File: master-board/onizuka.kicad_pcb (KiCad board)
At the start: 2 copper layers, 50 x 50 mm, 27 parts, among them IC1 FT232RQ, IC2 ADCMP371, P1 USB_OTG, P2 FTDI, P3 EXTRA, Q1 Q_PMOS_DGS, SW1 SWITCH_INV, U1 LD1117S33TR

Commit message: ESP8266 daughter board
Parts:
- moved R4 55.9 mm to (56.8, 25.4), turned to 270 degrees
- moved C3 50.5 mm to (45.8, 29.0), turned to 90 degrees
- moved SW1 49.5 mm to (55.2, 36.8)
- moved D2 48.9 mm to (43.6, 31.2), turned to 180 degrees
- moved R2 48.9 mm to (46.4, 31.2)
- moved D1 47.3 mm to (43.6, 32.8), turned to 180 degrees
- moved R1 47.3 mm to (46.4, 32.8)
- moved R6 46.2 mm to (51.4, 34.3)
- moved R5 45.9 mm to (48.8, 34.3)
- moved C2 45.7 mm to (47.4, 29.0), turned to 90 degrees
- moved IC2 43.8 mm to (50.2, 36.6), turned to 180 degrees
- moved C1 41.2 mm to (49.8, 26.7), turned to 180 degrees
- moved R3 38.8 mm to (34.5, 42.7), turned to 180 degrees
- moved D3 37.5 mm to (38.9, 43.1)
- moved U1 34.4 mm to (57.9, 41.9), turned to 270 degrees
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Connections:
- IC1 pad 33: (no net) -> GND
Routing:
- net +5V: track 0.00 -> 38.1 mm, vias 0 -> 4
- net /RI: track 0.00 -> 21.2 mm, vias 0 -> 2
- net /DCD: track 0.15 -> 21.3 mm, vias 0 -> 2
- net /VCCIO: track 0.00 -> 20.6 mm, vias 0 -> 2
- net /DSR: track 0.00 -> 19.4 mm, vias 0 -> 2
- net /TXD: track 0.15 -> 19.1 mm, vias 0 -> 1
- net GND: track 0.00 -> 17.8 mm, vias 0 -> 10
- net /DTR: track 0.00 -> 13.7 mm
- net /CTS: track 0.00 -> 12.4 mm
- net /RTS: track 1.32 -> 13.4 mm
- net /RXD: track 0.15 -> 10.7 mm
- net /PWROUT: track 3.07 -> 10.3 mm, vias 0 -> 1
- net +3V3: track 0.00 -> 6.40 mm
- net /PWREN: track 0.00 -> 4.51 mm
- net /TXLED: track 0.00 -> 4.34 mm
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- added copper zone on B.Cu, net GND

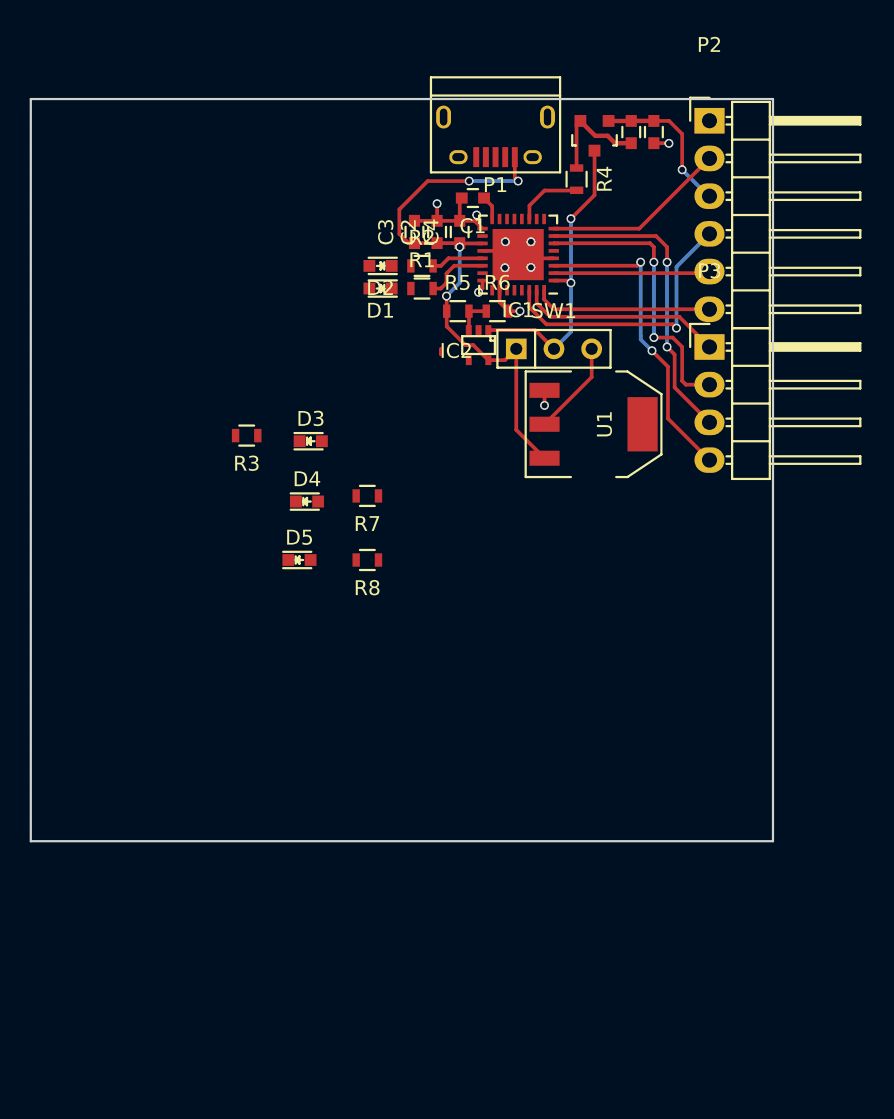
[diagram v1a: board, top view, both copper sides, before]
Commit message: Slight schematic rework, much PCB faffing
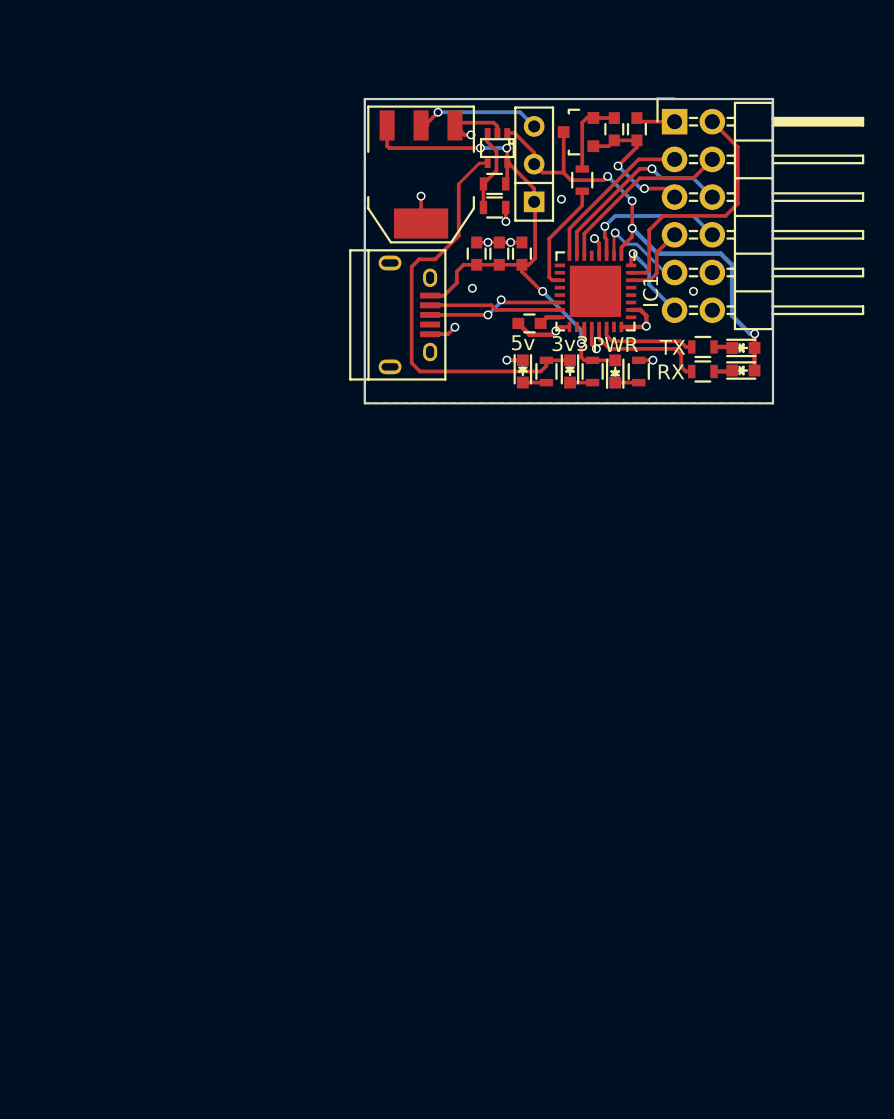
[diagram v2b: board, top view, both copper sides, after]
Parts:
- removed P3: EXTRA, Pin_Headers:Pin_Header_Angled_1x04
- P2: footprint Pin_Headers:Pin_Header_Angled_1x06 -> Pin_Headers:Pin_Header_Angled_2x06
- moved R3 26.8 mm to (61.0, 38.4), turned to 90 degrees
- moved D2 25.4 mm to (68.0, 38.3), turned to 0 degrees
- moved D1 24.8 mm to (68.0, 36.8), turned to 0 degrees
- moved D3 21.0 mm to (59.4, 38.4), turned to 90 degrees
- moved U1 20.4 mm to (46.3, 25.1), turned to 180 degrees
- moved R2 20.2 mm to (65.3, 38.4), turned to 180 degrees
- moved D4 19.8 mm to (56.3, 38.4), turned to 270 degrees
- moved D5 19.7 mm to (53.1, 38.4), turned to 270 degrees
- moved R1 19.3 mm to (65.3, 36.7), turned to 180 degrees
- moved R8 17.5 mm to (54.7, 38.4), turned to 270 degrees
- moved R7 17.3 mm to (57.8, 38.4), turned to 270 degrees
- moved P1 13.6 mm to (45.3, 34.5), turned to 270 degrees
- moved IC2 13.3 mm to (51.4, 23.3)
- moved SW1 12.5 mm to (53.9, 24.4), turned to 90 degrees
- moved C1 9.27 mm to (53.6, 35.1)
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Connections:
- IC1 pad 10: (no net) -> Net-(IC1-Pad10)
- IC1 pad 12: (no net) -> Net-(IC1-Pad12)
- IC1 pad 13: (no net) -> Net-(IC1-Pad13)
- IC1 pad 18: (no net) -> Net-(IC1-Pad18)
- IC1 pad 23: (no net) -> Net-(IC1-Pad23)
- IC1 pad 25: (no net) -> Net-(IC1-Pad25)
- IC1 pad 27: (no net) -> Net-(IC1-Pad27)
- IC1 pad 28: (no net) -> Net-(IC1-Pad28)
- IC1 pad 29: (no net) -> Net-(IC1-Pad29)
- IC1 pad 33: GND -> (no net)
- IC1 pad 5: (no net) -> Net-(IC1-Pad5)
- IC1 pad 9: (no net) -> Net-(IC1-Pad9)
- P1 pad 4: (no net) -> Net-(P1-Pad4)
- P1 pad 6: Net-(P1-Pad6) -> GND
- P2 pad 2: /CTS -> /DTR
- P2 pad 3: /PWROUT -> /CTS
- P2 pad 4: /TXD -> /DSR
- P2 pad 5: /RXD -> /PWROUT
- P2 pad 6: /RTS -> /DCD
- U1 pad 4: (no net) -> GND
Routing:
- net Net-(D4-Pad1): track 0.00 -> 28.0 mm
- net /TXD: track 19.1 -> 5.02 mm, vias 1 -> 0
- net /VCCIO: track 20.6 -> 33.5 mm, vias 2 -> 4
- net /RI: track 21.2 -> 10.1 mm, vias 2 -> 1
- net GND: track 17.8 -> 28.3 mm, vias 10 -> 15
- net Net-(IC1-Pad14): track 0.00 -> 9.78 mm, vias 0 -> 2
- net Net-(IC1-Pad15): track 0.00 -> 9.34 mm
- net /DCD: track 21.3 -> 13.3 mm, vias 2 -> 1
- net /RTS: track 13.4 -> 5.82 mm, vias 0 -> 1
- net /DSR: track 19.4 -> 12.2 mm, vias 2 -> 0
- net /RXLED: track 3.54 -> 8.42 mm
- net /RXD: track 10.7 -> 6.74 mm, vias 0 -> 1
- net Net-(IC2-Pad3): track 2.44 -> 5.66 mm
- net /DTR: track 13.7 -> 16.9 mm
- net /PWREN: track 4.51 -> 7.51 mm
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- added copper zone on F.Cu, net GND
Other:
- board size 50 x 50 mm -> 27.5 x 20.5 mm

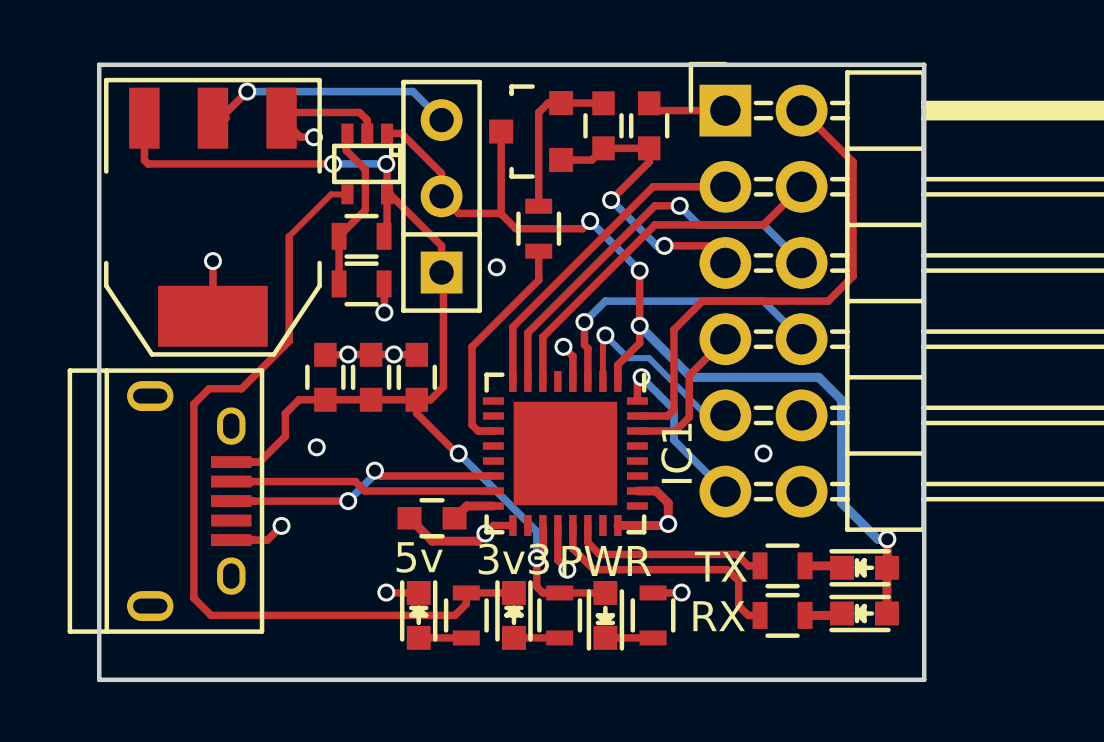
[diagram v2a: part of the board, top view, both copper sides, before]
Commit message: Various upgrades, also ESP-12E footprint for ESP board
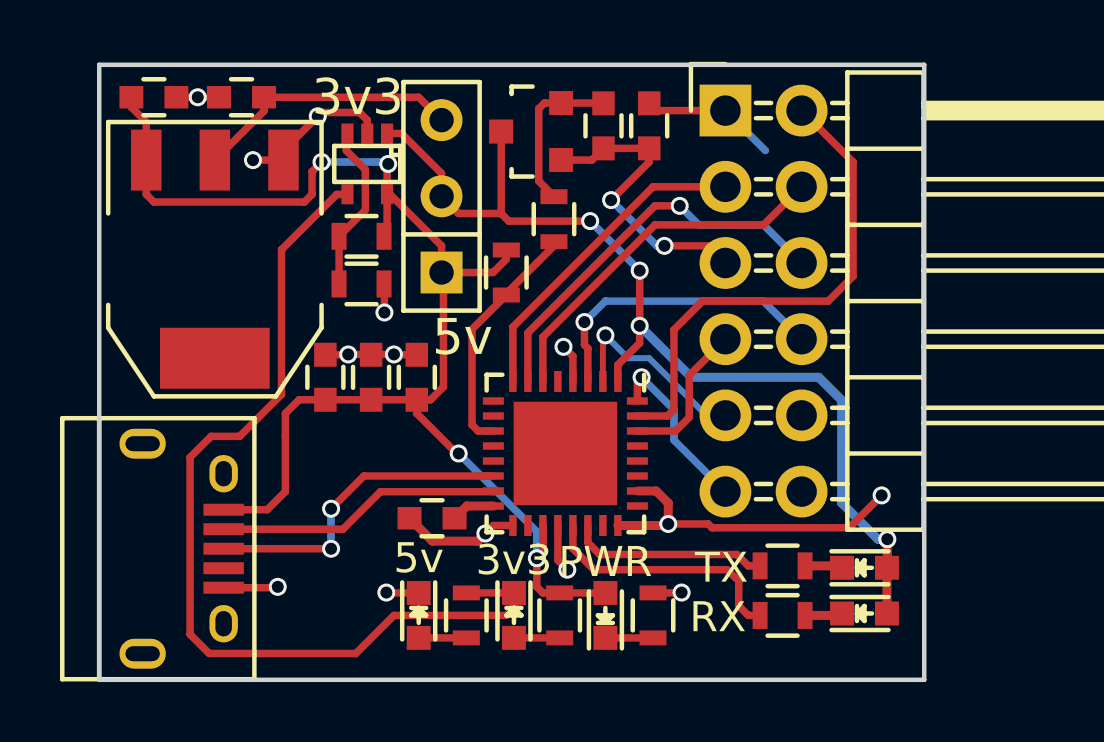
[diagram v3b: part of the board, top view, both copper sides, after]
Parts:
- added C7: 100n, Capacitors_SMD:C_0603, F.Cu at (44.3, 21.1)
- added C8: 10u, Capacitors_SMD:C_0603, F.Cu at (47.2, 21.1)
- added R9: 10k, Resistors_SMD:R_0603, F.Cu at (56.1, 26.9)
- moved P1 1.61 mm to (45.1, 36.1)
- moved U1 1.40 mm to (46.4, 26.5)
- moved R4 0.60 mm to (57.7, 25.1)
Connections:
- net Net-(D4-Pad1) renamed /LEDCTRL
- net Net-(IC1-Pad14) renamed /USBD+
- net Net-(IC1-Pad15) renamed /USBD-
- net Net-(IC2-Pad3) renamed /4v5
- U1 pad 4: GND -> (no net)
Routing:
- net GND: track 28.3 -> 37.2 mm, vias 15 -> 14
- net +5V: track 40.6 -> 47.9 mm
- net /LEDCTRL: track 28.0 -> 31.4 mm
- net /USBD+: track 9.78 -> 10.8 mm
- net /PWREN: track 7.51 -> 8.03 mm
- net +3V3: track 8.64 -> 9.01 mm, vias 1 -> 0
- removed copper zone on F.Cu, net GND
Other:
- board text added: "3v3"
- board text added: "5v"

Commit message: More faffing
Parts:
- moved C2 5.17 mm to (49.0, 35.5), turned to 270 degrees
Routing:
- net /USBD+: track 10.8 -> 10.00 mm
- net GND: vias 14 -> 13
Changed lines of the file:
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@@
     (links 70)
     (no_connects 0)
-    (area 42.424999 19.924999 70.075001 40.575001)
+    (area 39.16 15.3015 76.798001 41.229)
     (thickness 1.6)
     (drawings 6)
-    (tracks 272)
+    (tracks 269)
     (zones 0)
     (modules 29)
@@
   )
   (module Capacitors_SMD:C_0603 (layer F.Cu)
-    (at 50.038 30.4165 90)
+    (at 49.022 35.4838 270)
     (descr "Capacitor SMD 0603, reflow soldering, AVX (see smccp.pdf)")
     (tags "capacitor 0603")
     (attr smd)
-    (fp_text reference C2 (at 0 -1.9 90) (layer F.SilkS) hide
-      (effects (font (size 1 1) (thickness 0.15)))
-    )
-    (fp_text value 10n (at 0 1.9 90) (layer F.Fab) hide
+    (fp_text reference C2 (at 0 -1.9 270) (layer F.SilkS) hide
+      (effects (font (size 1 1) (thickness 0.15)))
+    )
+    (fp_text value 10n (at 0 1.9 270) (layer F.Fab) hide
       (effects (font (size 1 1) (thickness 0.15)))
     )
@@
     (fp_line (start -0.35 -0.6) (end 0.35 -0.6) (layer F.SilkS) (width 0.15))
     (fp_line (start 0.35 0.6) (end -0.35 0.6) (layer F.SilkS) (width 0.15))
-    (pad 1 smd rect (at -0.75 0 90) (size 0.8 0.75) (layers F.Cu F.Paste F.Mask)
+    (pad 1 smd rect (at -0.75 0 270) (size 0.8 0.75) (layers F.Cu F.Paste F.Mask)
       (net 3 +5V))
-    (pad 2 smd rect (at 0.75 0 90) (size 0.8 0.75) (layers F.Cu F.Paste F.Mask)
+    (pad 2 smd rect (at 0.75 0 270) (size 0.8 0.75) (layers F.Cu F.Paste F.Mask)
       (net 2 GND))
     (model Capacitors_SMD.3dshapes/C_0603.wrl
@@
   (segment (start 54.344 35.1155) (end 54.753 34.7065) (width 0.3) (layer F.Cu) (net 1))
   (segment (start 54.753 34.7065) (end 55.639 34.7065) (width 0.3) (layer F.Cu) (net 1))
+  (segment (start 46.65124 37.4269) (end 48.5521 37.4269) (width 0.25) (layer F.Cu) (net 2))
+  (segment (start 49.022 36.957) (end 48.5521 37.4269) (width 0.25) (layer F.Cu) (net 2))
+  (via (at 48.5521 37.4269) (size 0.6) (drill 0.4) (layers F.Cu B.Cu) (net 2))
+  (segment (start 49.022 36.957) (end 49.022 36.2338) (width 0.25) (layer F.Cu) (net 2))
+  (segment (start 46.65124 37.4269) (end 46.64754 37.4306) (width 0.25) (layer F.Cu) (net 2))
   (segment (start 61.468 35.306) (end 62.8015 35.306) (width 0.25) (layer F.Cu) (net 2))
   (via (at 68.58 34.3535) (size 0.6) (drill 0.4) (layers F.Cu B.Cu) (net 2))
@@
   (via (at 45.7835 21.082) (size 0.6) (drill 0.4) (layers F.Cu B.Cu) (net 2))
   (segment (start 45.7835 21.082) (end 45.073 21.082) (width 0.25) (layer F.Cu) (net 2))
-  (segment (start 46.64754 37.4306) (end 48.4214 37.4306) (width 0.25) (layer F.Cu) (net 2))
-  (via (at 48.4505 37.4015) (size 0.6) (drill 0.4) (layers F.Cu B.Cu) (net 2))
-  (segment (start 48.4214 37.4306) (end 48.4505 37.4015) (width 0.25) (layer F.Cu) (net 2))
   (segment (start 57.789 35.3565) (end 57.789 36.5165) (width 0.25) (layer F.Cu) (net 2))
   (via (at 58.1025 36.83) (size 0.6) (drill 0.4) (layers F.Cu B.Cu) (net 2))
@@
   (via (at 52.324 29.6545) (size 0.6) (drill 0.4) (layers F.Cu B.Cu) (net 2))
   (segment (start 52.336 29.6665) (end 53.086 29.6665) (width 0.25) (layer F.Cu) (net 2) (status 20))
-  (segment (start 51.574 29.6545) (end 50.8 29.6545) (width 0.25) (layer F.Cu) (net 2) (status 10))
-  (segment (start 50.038 29.6665) (end 50.788 29.6665) (width 0.25) (layer F.Cu) (net 2) (status 10))
-  (via (at 50.8 29.6545) (size 0.6) (drill 0.4) (layers F.Cu B.Cu) (net 2))
-  (segment (start 50.788 29.6665) (end 50.8 29.6545) (width 0.25) (layer F.Cu) (net 2))
   (segment (start 60.833 21.2845) (end 61.075 21.5265) (width 0.25) (layer F.Cu) (net 2) (status 30))
   (segment (start 61.075 21.5265) (end 63.373 21.5265) (width 0.25) (layer F.Cu) (net 2) (status 30))
@@
   (via (at 57.9755 29.4005) (size 0.6) (drill 0.4) (layers F.Cu B.Cu) (net 2))
   (segment (start 58.289 29.714) (end 57.9755 29.4005) (width 0.25) (layer F.Cu) (net 2))
+  (segment (start 49.022 34.7338) (end 49.022 32.0675) (width 0.25) (layer F.Cu) (net 3))
+  (segment (start 49.923 31.1665) (end 51.562 31.1665) (width 0.25) (layer F.Cu) (net 3))
+  (segment (start 49.022 32.0675) (end 49.923 31.1665) (width 0.25) (layer F.Cu) (net 3))
+  (segment (start 46.64754 34.8306) (end 48.9252 34.8306) (width 0.25) (layer F.Cu) (net 3))
+  (segment (start 48.9252 34.8306) (end 49.022 34.7338) (width 0.25) (layer F.Cu) (net 3))
   (segment (start 52.0954 24.3205) (end 52.0954 23.3426) (width 0.25) (layer F.Cu) (net 3))
   (segment (start 44.069 24.3205) (end 44.069 23.1775) (width 0.25) (layer F.Cu) (net 3))
@@
   (segment (start 44.069 21.9075) (end 43.573 21.4115) (width 0.25) (layer F.Cu) (net 3))
   (segment (start 43.573 21.4115) (end 43.573 21.082) (width 0.25) (layer F.Cu) (net 3))
-  (segment (start 46.64754 34.8306) (end 48.1004 34.8306) (width 0.25) (layer F.Cu) (net 3))
-  (segment (start 48.7045 32.385) (end 48.7045 31.623) (width 0.25) (layer F.Cu) (net 3))
-  (segment (start 48.7045 31.623) (end 49.161 31.1665) (width 0.25) (layer F.Cu) (net 3))
-  (segment (start 49.161 31.1665) (end 50.038 31.1665) (width 0.25) (layer F.Cu) (net 3) (status 20))
-  (segment (start 48.7045 34.2265) (end 48.7045 32.385) (width 0.25) (layer F.Cu) (net 3))
-  (segment (start 48.1004 34.8306) (end 48.7045 34.2265) (width 0.25) (layer F.Cu) (net 3))
   (segment (start 53.9115 26.924) (end 55.626 26.924) (width 0.25) (layer F.Cu) (net 3))
   (segment (start 56.0705 26.4795) (end 56.0705 26.174) (width 0.25) (layer F.Cu) (net 3))
@@
   (segment (start 53.975 26.9875) (end 53.9115 26.924) (width 0.25) (layer F.Cu) (net 3) (status 30))
   (segment (start 51.562 31.1665) (end 53.086 31.1665) (width 0.25) (layer F.Cu) (net 3) (status 30))
-  (segment (start 50.038 31.1665) (end 51.562 31.1665) (width 0.25) (layer F.Cu) (net 3) (status 30))
   (segment (start 60.833 22.7845) (end 60.833 23.241) (width 0.25) (layer F.Cu) (net 4) (status 10))
   (segment (start 61.341 26.035) (end 62.8015 26.035) (width 0.25) (layer F.Cu) (net 4) (status 20))
@@
   (via (at 60.579 30.4165) (size 0.6) (drill 0.4) (layers F.Cu B.Cu) (net 23))
   (segment (start 60.439 30.5565) (end 60.579 30.4165) (width 0.25) (layer F.Cu) (net 23))
-  (segment (start 46.64754 36.1306) (end 50.2276 36.1306) (width 0.25) (layer F.Cu) (net 38))
-  (segment (start 51.32 33.7065) (end 55.639 33.7065) (width 0.25) (layer F.Cu) (net 38))
-  (segment (start 50.2285 34.798) (end 51.32 33.7065) (width 0.25) (layer F.Cu) (net 38))
-  (via (at 50.2285 34.798) (size 0.6) (drill 0.4) (layers F.Cu B.Cu) (net 38))
-  (segment (start 50.2285 36.1315) (end 50.2285 34.798) (width 0.25) (layer B.Cu) (net 38))
-  (via (at 50.2285 36.1315) (size 0.6) (drill 0.4) (layers F.Cu B.Cu) (net 38))
-  (segment (start 50.2276 36.1306) (end 50.2285 36.1315) (width 0.25) (layer F.Cu) (net 38))
+  (segment (start 46.64754 36.1306) (end 48.0051 36.1306) (width 0.25) (layer F.Cu) (net 38))
+  (segment (start 51.2565 33.7065) (end 55.639 33.7065) (width 0.25) (layer F.Cu) (net 38))
+  (segment (start 50.2285 34.7345) (end 51.2565 33.7065) (width 0.25) (layer F.Cu) (net 38))
+  (via (at 50.2285 34.7345) (size 0.6) (drill 0.4) (layers F.Cu B.Cu) (net 38))
+  (segment (start 49.403 34.7345) (end 50.2285 34.7345) (width 0.25) (layer B.Cu) (net 38))
+  (segment (start 48.006 36.1315) (end 49.403 34.7345) (width 0.25) (layer B.Cu) (net 38))
+  (via (at 48.006 36.1315) (size 0.6) (drill 0.4) (layers F.Cu B.Cu) (net 38))
+  (segment (start 48.0051 36.1306) (end 48.006 36.1315) (width 0.25) (layer F.Cu) (net 38))
   (segment (start 46.64754 35.4806) (end 50.6254 35.4806) (width 0.25) (layer F.Cu) (net 39))
   (segment (start 51.874502 34.231498) (end 55.639 34.231498) (width 0.25) (layer F.Cu) (net 39))
